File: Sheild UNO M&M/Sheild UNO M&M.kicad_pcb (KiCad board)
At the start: 2 copper layers, 68.6 x 53.3 mm, 24 parts, among them J1 Power, J2 Analog, J3 Digital/PWM, J4 Digital/PWM, J5 Conn_01x02, J6 Conn_01x02, U1 HC05, U2 MCP41050, U4 LTC1050

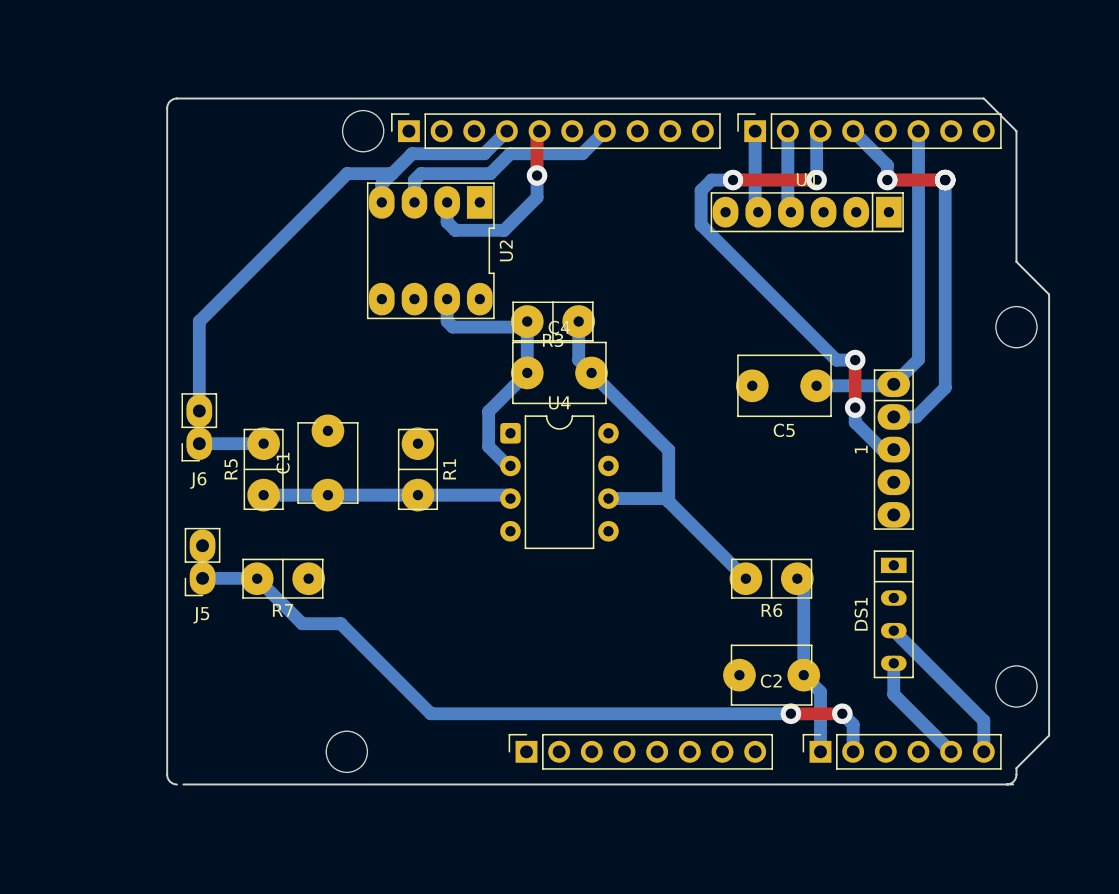
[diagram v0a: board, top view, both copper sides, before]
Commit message: Correction de l'erreur du GND connecté au 5V, continuer le routage
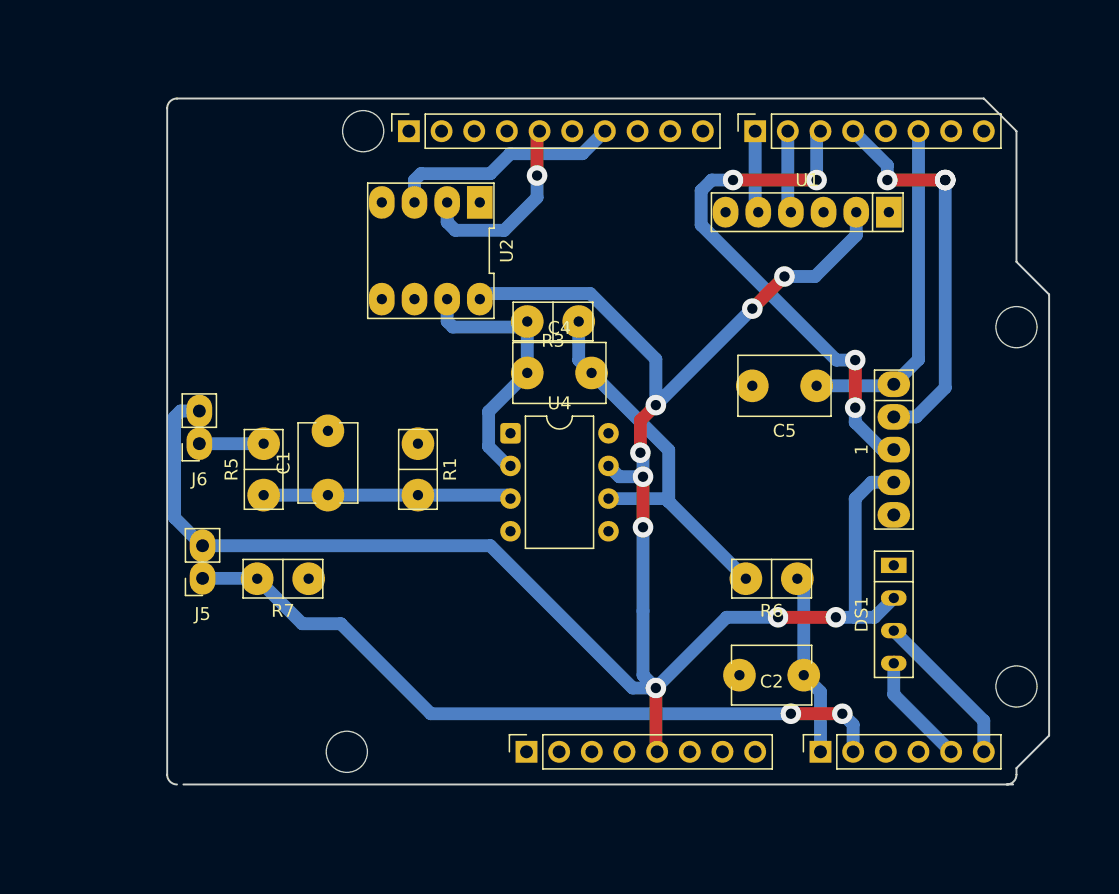
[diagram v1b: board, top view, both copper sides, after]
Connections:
- 1 pad 5: 5V -> GND
- C1 pad 2: 5V -> GND
- C2 pad 2: 5V -> GND
- C5 pad 2: 5V -> GND
- DS1 pad 1: 5V -> GND
- J1 pad 6: 5V -> GND
- J1 pad 7: 5V -> GND
- J3 pad 4: 5V -> GND
- R1 pad 2: 5V -> GND
- R7 pad 2: 5V -> GND
- U1 pad 3: 5V -> GND
- U2 pad 4: 5V -> GND
- U2 pad 5: 5V -> GND
- U2 pad 6: 5V -> GND
- U4 pad 4: 5V -> GND
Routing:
- net 5V: track 39.6 -> 160.4 mm, vias 0 -> 9

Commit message: Corrections PCB sur les empreintes des connecteurs et amélioration des via
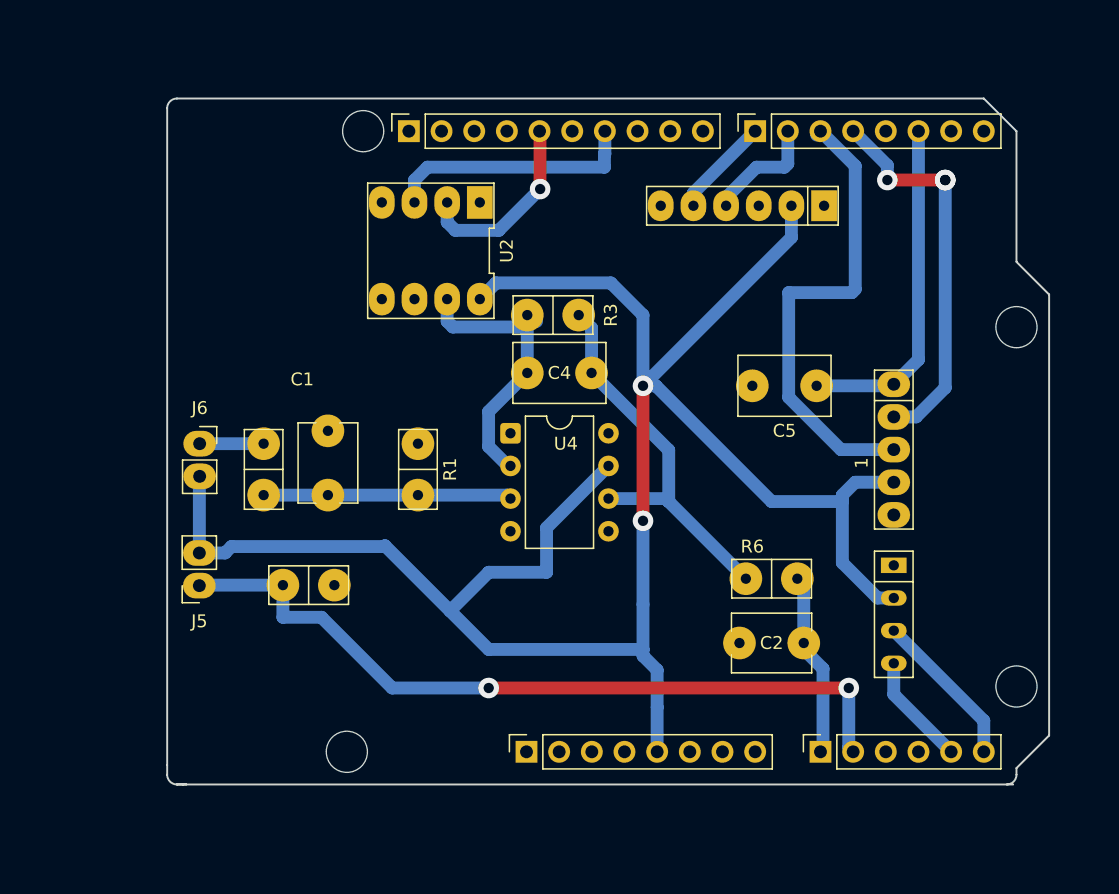
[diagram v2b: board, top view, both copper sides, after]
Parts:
- J5, J6: footprint Une_Librairie_d_empreinte:PinSocket_1x02_P2.54mm_Vertical_Header_Empreinte -> Une_Librairie_d_empreinte:PinSocket_1x02_P2.54mm_Vertical_Modifié
- moved U1 5.06 mm to (144.7, 55.0)
- moved C2 2.50 mm to (149.5, 89.0)
- moved R7 2.06 mm to (111.0, 84.5)
- moved J5 0.62 mm to (102.5, 84.5)
- moved R3 0.50 mm to (130.0, 63.5)
- turned J6 to 0 degrees
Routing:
- net 5V: track 160.4 -> 164.7 mm, vias 9 -> 2
- net SW: track 41.0 -> 37.1 mm, vias 4 -> 0
- net A1: track 57.4 -> 60.4 mm
- net Tx: track 6.40 -> 9.06 mm
- net SI: track 18.1 -> 19.7 mm
- net Rx: track 6.40 -> 7.79 mm
- net Net-(C4-Pad2): track 30.2 -> 30.7 mm
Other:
- outline, holes or cut-outs redrawn

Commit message: Correction PCB et ajout des modèles 3D
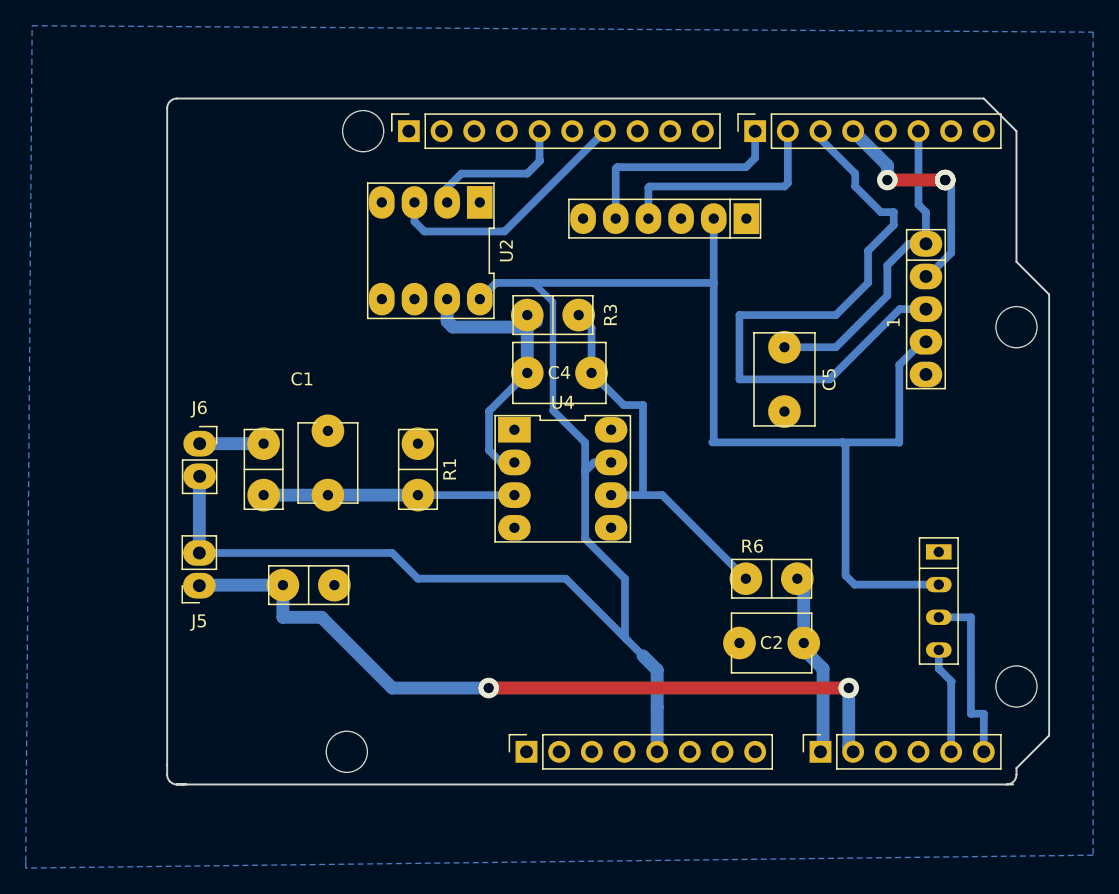
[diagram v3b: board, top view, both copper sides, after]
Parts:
- U4: footprint Package_DIP:DIP-8_W7.62mm -> Une_Librairie_d_empreinte:Potentiometre MCP41050
- moved 1 11.2 mm to (159.0, 63.0)
- moved U1 6.12 mm to (138.7, 56.0)
- moved U4 5.39 mm to (130.8, 76.2), turned to -90 degrees
- moved C5 3.91 mm to (148.0, 66.0), turned to -90 degrees
- moved DS1 3.65 mm to (160.0, 85.7)
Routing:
- net DT: track 30.5 -> 18.0 mm
- net SW: track 37.1 -> 48.6 mm
- net Rx: track 7.79 -> 17.1 mm
- net Tx: track 9.06 -> 17.4 mm
- net SCK: track 15.2 -> 12.0 mm, vias 2 -> 0
- net 5V: track 164.7 -> 162.4 mm, vias 2 -> 0
- net CLK: track 26.5 -> 24.7 mm
- net SCL: track 12.3 -> 14.0 mm
- net Net-(U4-+): track 19.3 -> 19.9 mm
- net Net-(C4-Pad2): track 30.7 -> 30.1 mm
- added copper zone on B.Cu, net GND

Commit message: Finalisation du shield
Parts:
- moved U1 0.51 mm to (138.8, 56.5)
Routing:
- net GND: track 0.00 -> 16.5 mm, vias 0 -> 2
- net CS: track 0.00 -> 15.9 mm, vias 0 -> 2
- net 5V: track 162.4 -> 167.3 mm
- net SI: track 19.8 -> 22.8 mm
- net SW: track 48.6 -> 46.0 mm
- net Tx: track 17.4 -> 16.4 mm
- net CLK: track 24.7 -> 24.0 mm
- net R2: track 22.7 -> 22.1 mm

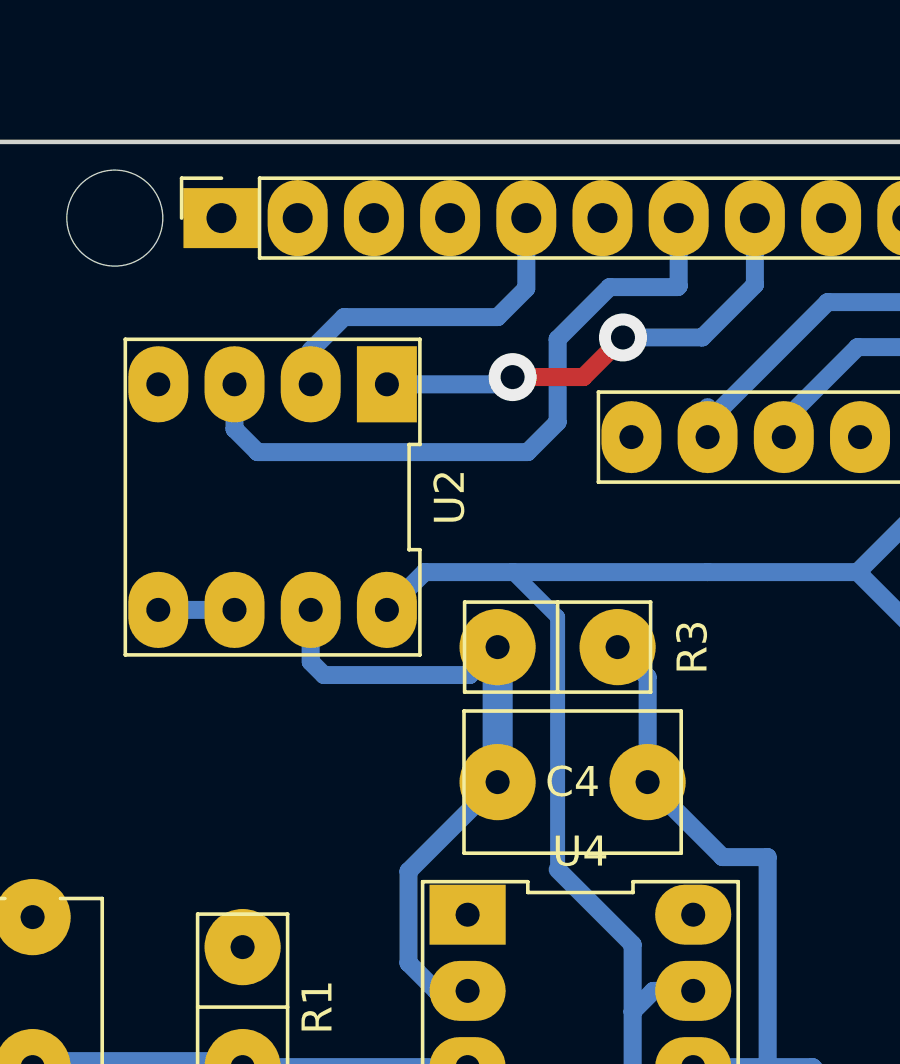
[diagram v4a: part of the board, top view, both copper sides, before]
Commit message: Rajout d'une image de la simulation du LTSpice
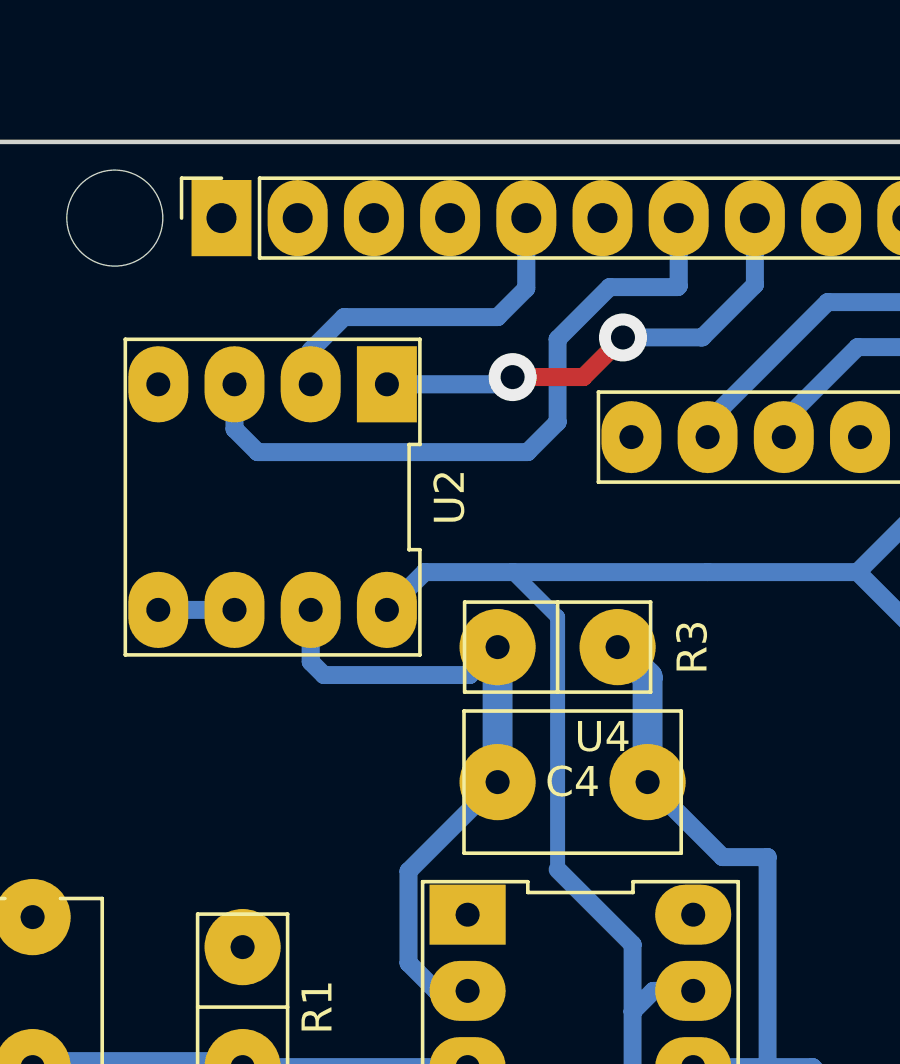
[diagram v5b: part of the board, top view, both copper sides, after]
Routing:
- net Rx: track 16.8 -> 15.3 mm
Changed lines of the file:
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@@
 		(pad "1" thru_hole rect
 			(at 0 0 90)
-			(size 2 2.54)
+			(size 2.54 2)
 			(drill 1)
 			(layers "*.Cu" "*.Mask")
@@
 		(at 130.76 76.23 -90)
 		(property "Reference" "U4"
-			(at -5.91 0 0)
+			(at -9.73 -0.74 0)
 			(layer "F.SilkS")
 			(effects
@@
 		(start 133 64.5)
 		(end 132 63.5)
-		(width 0.6)
+		(width 1)
+		(layer "B.Cu")
+		(net 19)
+	)
+	(segment
+		(start 133 68)
+		(end 133 64.5)
+		(width 1)
 		(layer "B.Cu")
 		(net 19)
@@
 	)
 	(segment
-		(start 133 68)
-		(end 133 64.5)
-		(width 0.6)
-		(layer "B.Cu")
-		(net 19)
-	)
-	(segment
 		(start 137 77.5)
 		(end 137 70.5)
@@
 	)
 	(segment
-		(start 139 52)
-		(end 135 56)
+		(start 135 56)
+		(end 135 56.5)
 		(width 0.6)
 		(layer "B.Cu")
@@
 	)
 	(segment
-		(start 135 56)
-		(end 135 56.5)
+		(start 139 52)
+		(end 135 56)
 		(width 0.6)
 		(layer "B.Cu")
@@
 		(width 0.6)
 		(layer "B.Cu")
-		(net 29)
-	)
-	(segment
-		(start 135 55.5)
-		(end 135 57)
-		(width 0.6)
-		(layer "B.Cu")
